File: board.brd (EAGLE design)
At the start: 72 x 24 mm, 26 parts, among them IC1 74HCT125D, J1 M5STICK_PINOUT, J2 JST-SH 4 Position Connector, J3 USB_A_PTH_MALE

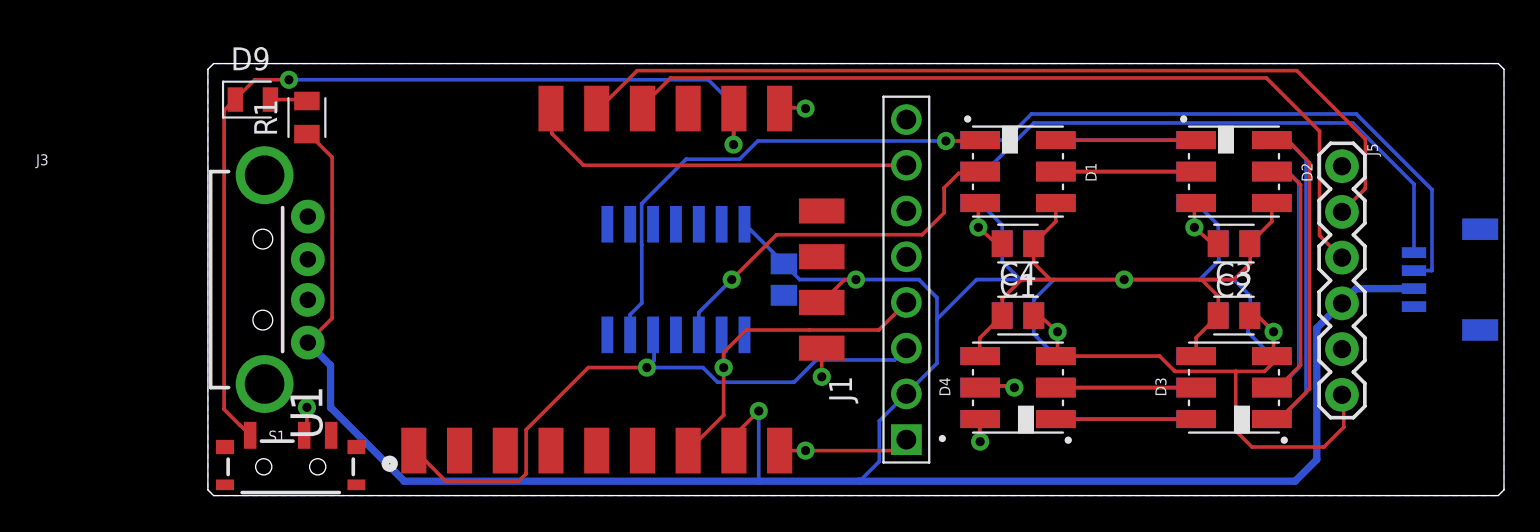
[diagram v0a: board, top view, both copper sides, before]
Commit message: fixed silkscreen for all components
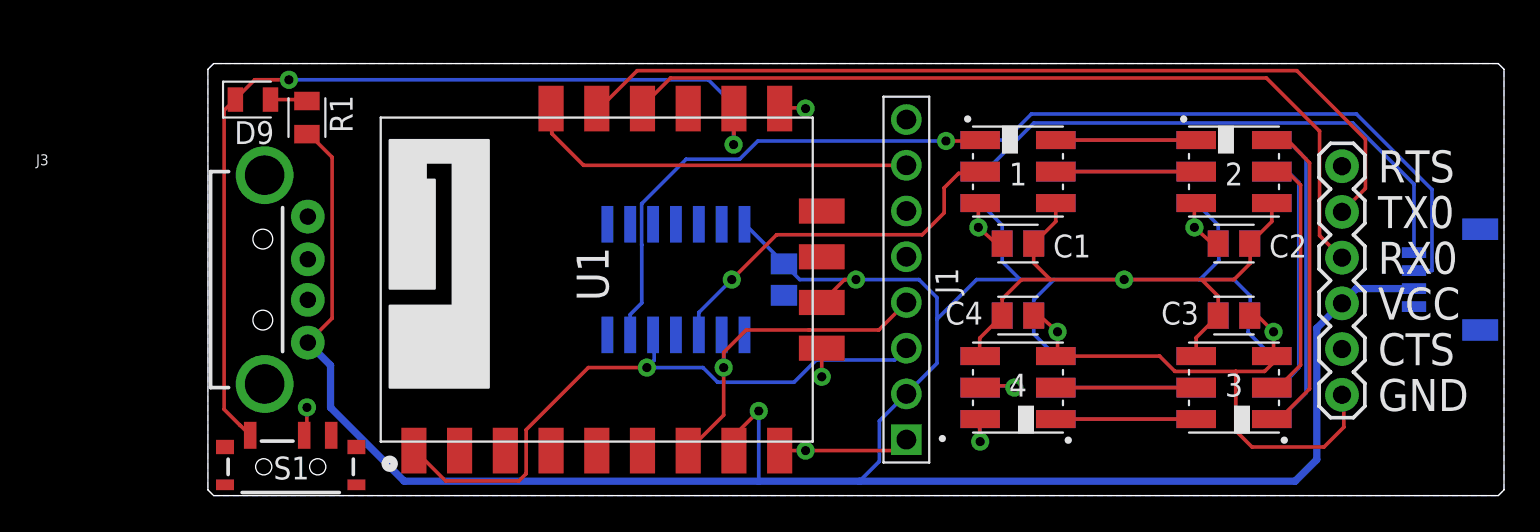
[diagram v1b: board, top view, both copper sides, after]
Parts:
- removed D1, D2, D3, D4, D5, D6, D7, D8: APA102-5050, SparkFun-LED:APA102-5050
- added 1, 2, 3, 4, 5, 6, 7, 8: APA102-5050, SparkFun-LED:APA102-5050
- C1, C2, C3, C4, C5, C6, C7, C8, C9: value (none) -> 0.1uF
- J5: value (none) -> SERIAL
- R1: value (none) -> 330
- S1: value (none) -> FLASH
- U1: value (none) -> M5STAMP PICO
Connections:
- net CI$1: now also 1.P2; no longer D1.P2
- net CI$2: now also 1.P5, 2.P2; no longer D1.P5, D2.P2
- net CI$3: now also 2.P5, 3.P2; no longer D2.P5, D3.P2
- net CI$4: now also 3.P5, 4.P2; no longer D3.P5, D4.P2
- net CI$5: now also 4.P5, 5.P2; no longer D4.P5, D5.P2
- net CI$6: now also 5.P5, 6.P2; no longer D5.P5, D6.P2
- net CI$7: now also 6.P5, 7.P2; no longer D6.P5, D7.P2
- net CI$8: now also 7.P5, 8.P2; no longer D7.P5, D8.P2
- net CO: now also 8.P5; no longer D8.P5
- net DI$1: now also 1.P1; no longer D1.P1
- net DI$2: now also 1.P6, 2.P1; no longer D1.P6, D2.P1
- net DI$3: now also 2.P6, 3.P1; no longer D2.P6, D3.P1
- net DI$4: now also 3.P6, 4.P1; no longer D3.P6, D4.P1
- net DI$5: now also 4.P6, 5.P1; no longer D4.P6, D5.P1
- net DI$6: now also 5.P6, 6.P1; no longer D5.P6, D6.P1
- net DI$7: now also 6.P6, 7.P1; no longer D6.P6, D7.P1
- net DI$8: now also 7.P6, 8.P1; no longer D7.P6, D8.P1
- net DO: now also 8.P6; no longer D8.P6
- net GND: now also 1.P3, 2.P3, 3.P3, 4.P3, 5.P3, 6.P3, 7.P3, 8.P3; no longer D1.P3, D2.P3, D3.P3, D4.P3, D5.P3, D6.P3, D7.P3, D8.P3
- net VCC: now also 1.P4, 2.P4, 3.P4, 4.P4, 5.P4, 6.P4, 7.P4, 8.P4; no longer D1.P4, D2.P4, D3.P4, D4.P4, D5.P4, D6.P4, D7.P4, D8.P4
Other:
- board text added: "CTS"
- board text added: "GND"
- board text added: "RTS"
- board text added: "RX0"
- board text added: "TX0"
- board text added: "VCC"
